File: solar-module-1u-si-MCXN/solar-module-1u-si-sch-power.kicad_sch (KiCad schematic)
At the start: 61 parts, among them J1 MMS-104-01-[F/L]-SH, Q1 NTR4101P, Q2 DMP2240UDM-7, U10 TPS63060DSCR, U12 LTC4412, U3 LT1618EMSTRPBF, U4 INA226

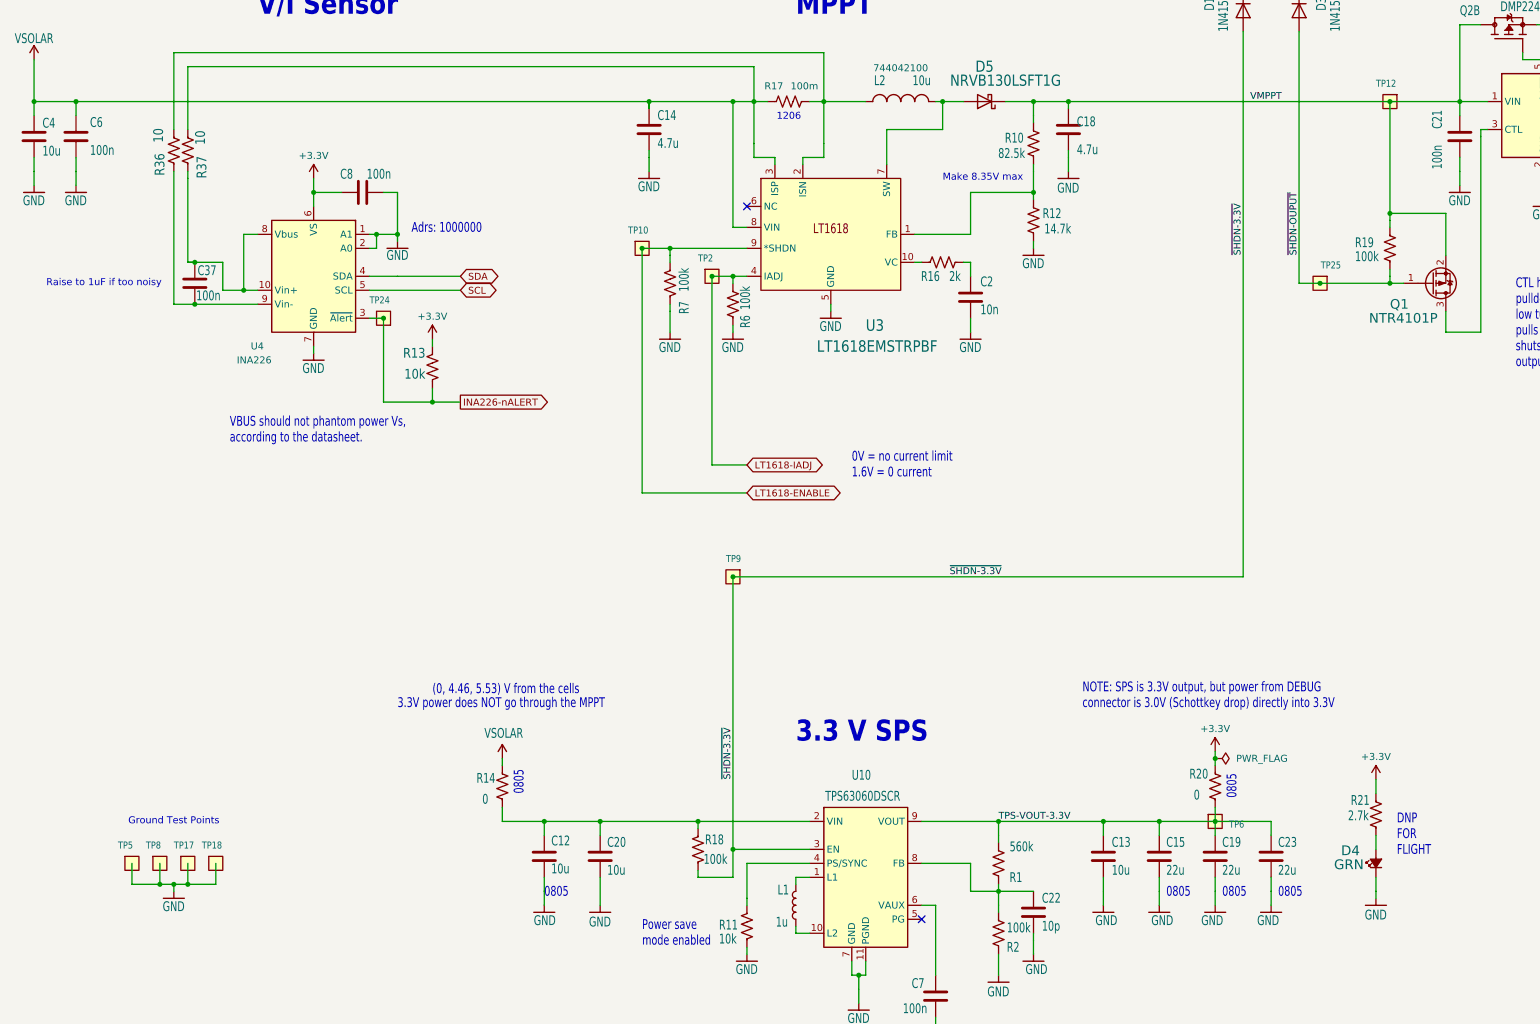
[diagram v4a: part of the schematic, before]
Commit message: Final polishing before fab. Fixed I2C pullups, removed some silly test points, lots of good zone planning on layer 3, cleaned up solar ideal diodes, moved LED to a blink light instead of power light.
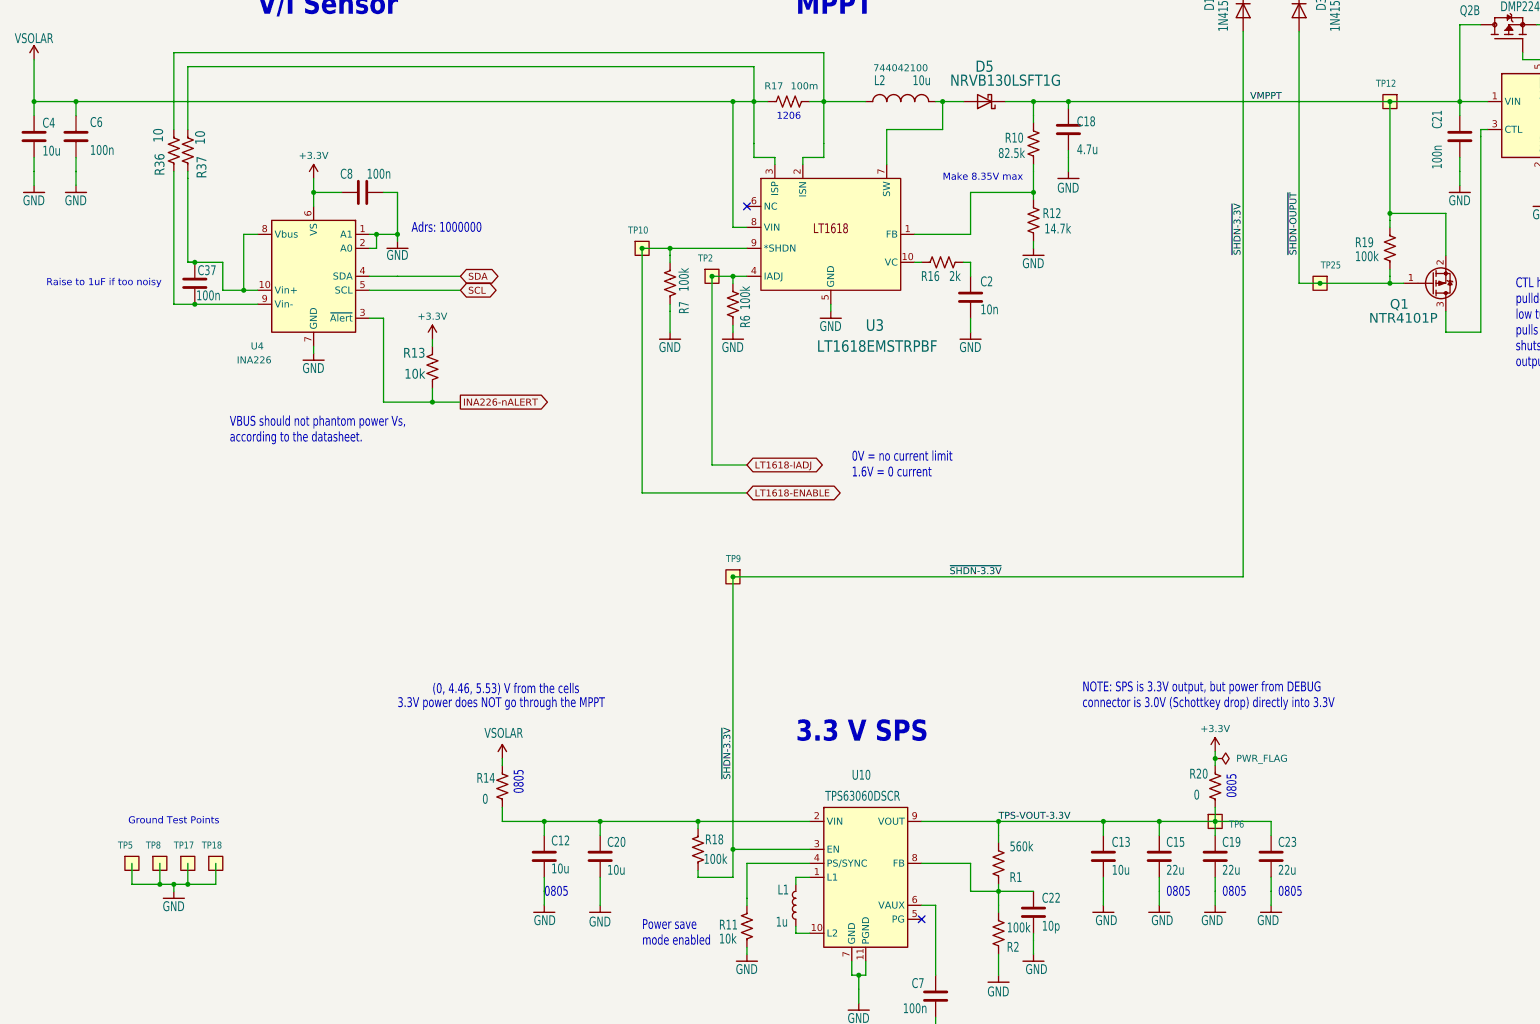
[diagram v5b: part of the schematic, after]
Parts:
- removed C14: 4.7u, oresat-passives:0603-C-NOSILK, symbol Device:C
- removed D4: GRN, LED_SMD:LED_0603_1608Metric, symbol Device:LED_Small_Filled
- removed R21: 2.7k, oresat-passives:0603-C-NOSILK, symbol Device:R_US
- removed TP24: TEST-POINT-LARGE-SQUARE, oresat-misc:TestPoint-0.75mm-th, symbol oresat-misc:Test-Point-0.75mm-th
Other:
- note removed: "DNP FOR FLIGHT"
- title: OreSat Solar Module - Silicon Cells -> OreSat Solar Module - Silicon Cells + MCXN

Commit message: Fix up BOM
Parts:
- C12, C13, C2, C20, C22, C4, CF1, D1, D3, D5, L1, L2, Q2, R1, R10, R18, R19, R2, R36, R37, R6, R7, U10, U12, U3, U4: DIS Digi-Key -> DIgiKey
- C15, C19, C23: DIS Digi-Key -> DigiKey; DPN GRT21BR61E226ME13L -> 490-9959-1-ND; MFR Murata -> Murata Electronics; MPN 490-12389-2-ND -> GRM21BR61E226ME44L
- C18: DIS Digi-Key -> DigiKey; DPN 1276-1784-1-ND -> 587-4332-1-ND; MFR Samsung Electro-Mechanics -> Taiyo Yuden; MPN CL10A475KO8NNNC -> EMK107BBJ475KAHT
- C21, C37, C6, C7, C8, R11, R13: DIS Digi-Key -> DigiKey
- J1: DIS Digi-Key -> DIgiKey; DPN SAM1237-04-ND -> MMS-104-02-L-SH-ND
- Q1: DIS (none) -> DIgiKey
